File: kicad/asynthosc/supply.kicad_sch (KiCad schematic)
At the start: 50 parts, among them J1 USB_B_Micro, J2 Conn_02x05_Odd_Even, U1 LM1117S-3.3, U2 LMR62421XMF, U3 USBLC6-2SC6, U4 LM1117S-5.0, U5 Si1869DH

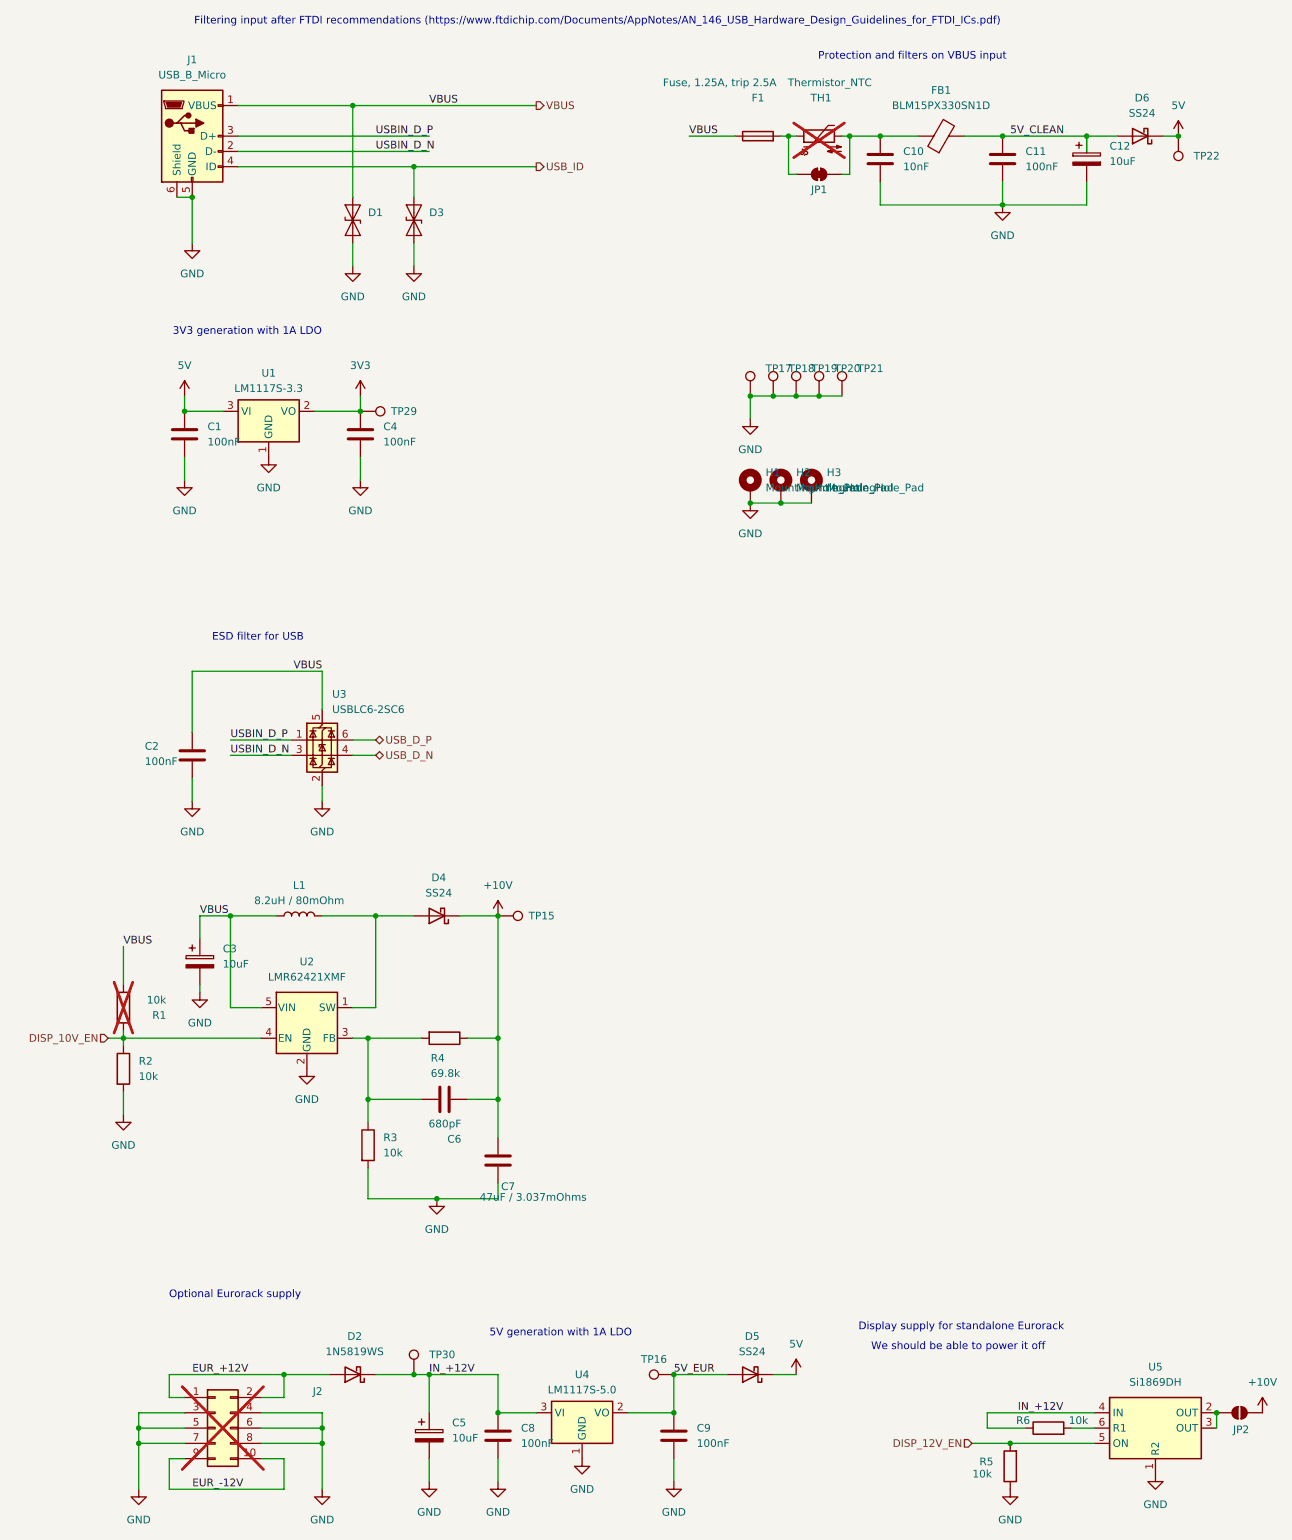
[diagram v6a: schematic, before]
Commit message: pcb: route, add some silkscreen
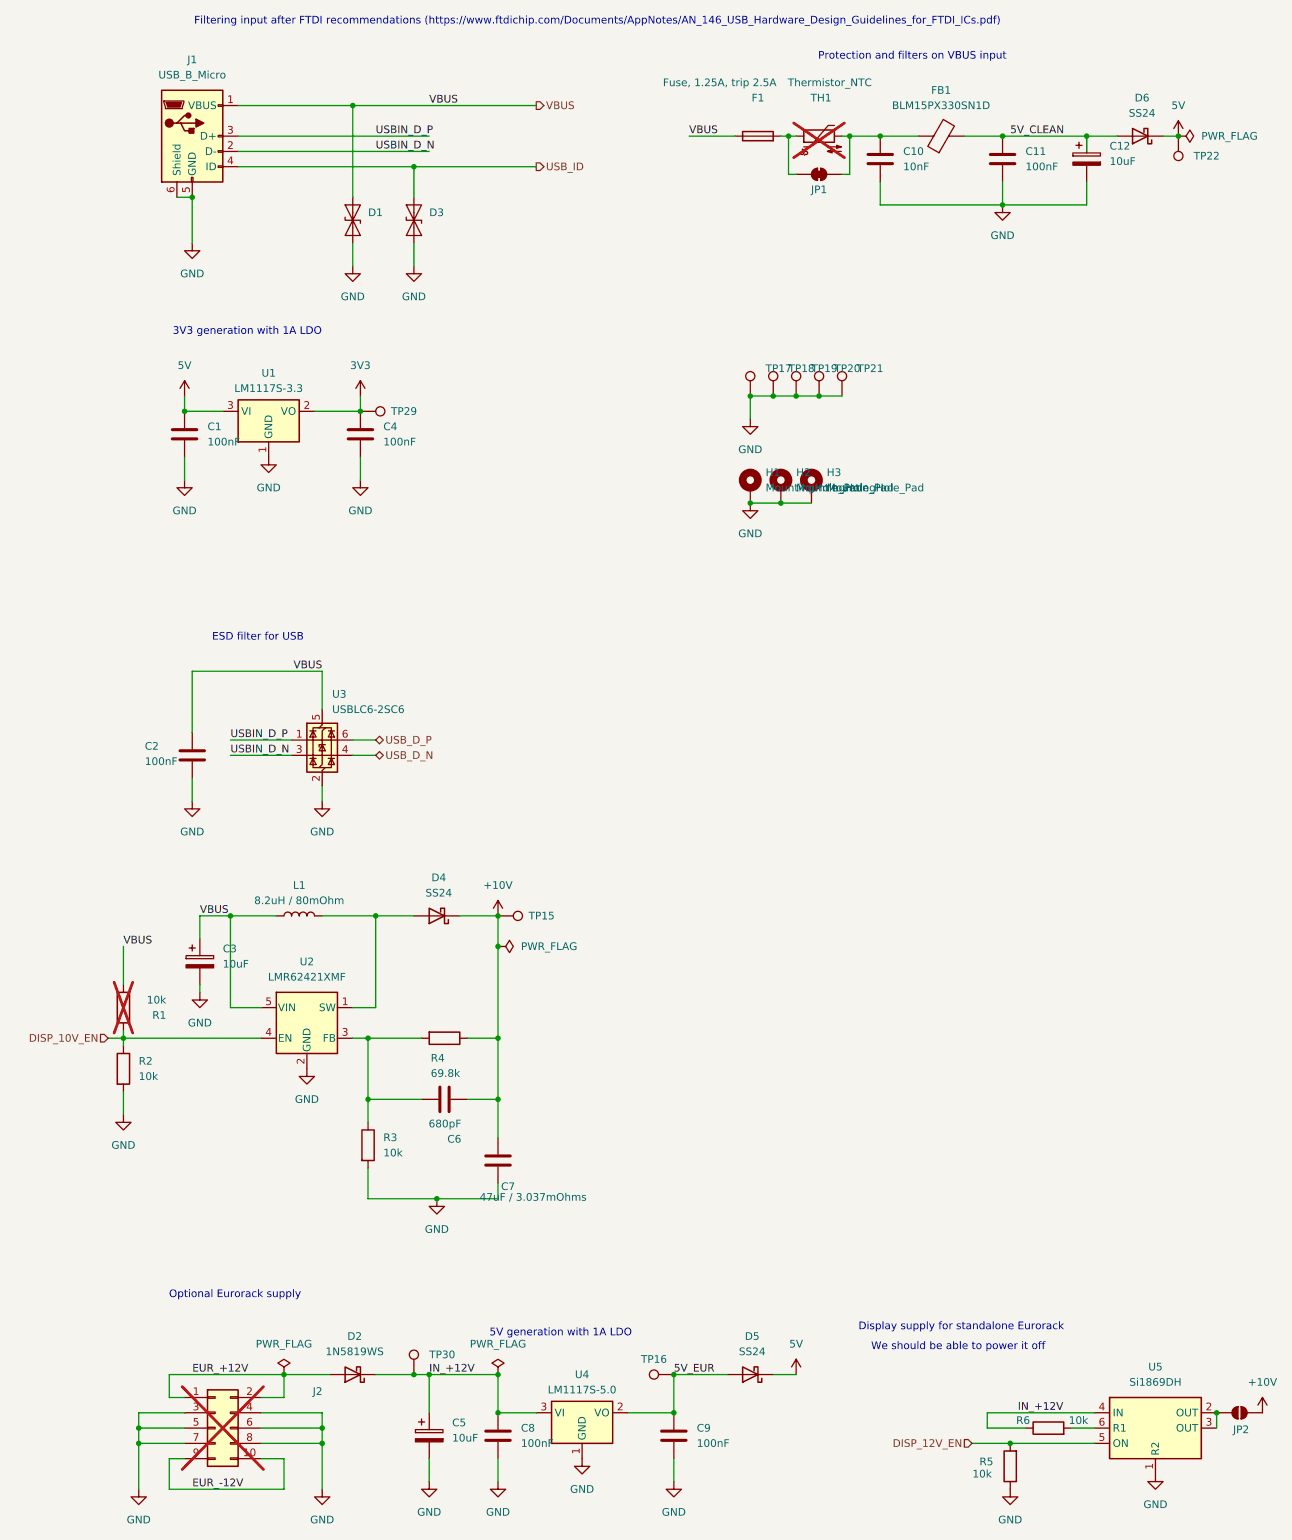
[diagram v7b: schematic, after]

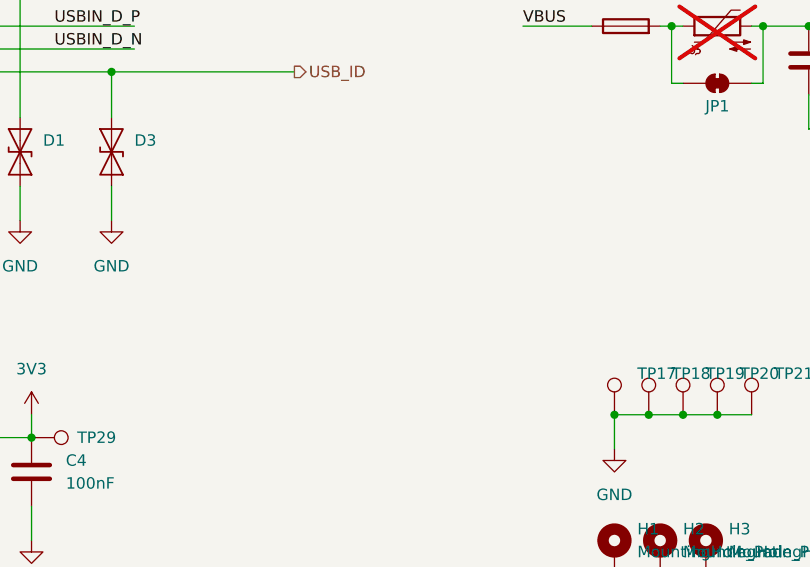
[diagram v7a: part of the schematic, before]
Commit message: comp: add vertical usb micro-b and rj45 footprints
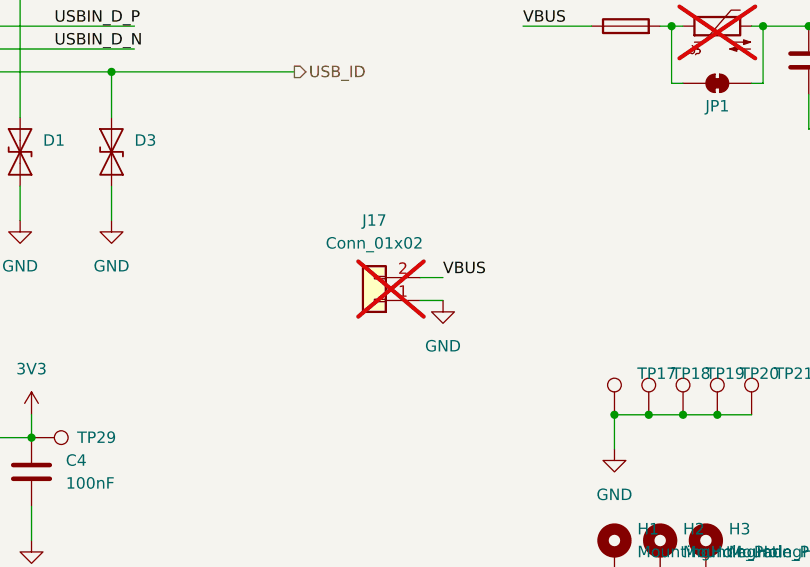
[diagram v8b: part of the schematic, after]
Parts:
- added J17: Conn_01x02, Connector_PinHeader_2.54mm:PinHeader_1x02_P2.54mm_Vertical, symbol Connector_Generic:Conn_01x02
- J1: footprint asynthosc:USB_Micro-B_Shou-han-MicroXNJ -> asynthosc:USB_Micro-B_Hanxia_HX_MICRO_180D_ZB; Manufacturer ShouHan -> Hanxia; RefNum MicroXNJ -> HX MICRO 180D ZB
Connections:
- net GND: now also J17.1 (Pin_1)
- net VBUS: now also J17.2 (Pin_2)
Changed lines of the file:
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@@
 	(wire
 		(pts
+			(xy 111.76 71.12) (xy 114.3 71.12)
+		)
+		(stroke
+			(width 0)
+			(type default)
+		)
+	)
+	(wire
+		(pts
 			(xy 67.31 60.96) (xy 67.31 64.77)
 		)
@@
 	(wire
 		(pts
+			(xy 111.76 73.66) (xy 114.3 73.66)
+		)
+		(stroke
+			(width 0)
+			(type default)
+		)
+	)
+	(wire
+		(pts
 			(xy 154.94 50.8) (xy 154.94 54.61)
 		)
@@
 	)
 	(label "VBUS"
+		(at 114.3 71.12 0)
+		(fields_autoplaced yes)
+		(effects
+			(font
+				(size 1.27 1.27)
+			)
+			(justify left bottom)
+		)
+	)
+	(label "VBUS"
 		(at 80.01 38.1 0)
 		(fields_autoplaced yes)
@@
 	)
 	(symbol
+		(lib_id "Connector_Generic:Conn_01x02")
+		(at 106.68 73.66 180)
+		(unit 1)
+		(exclude_from_sim yes)
+		(in_bom no)
+		(on_board yes)
+		(dnp yes)
+		(fields_autoplaced yes)
+		(property "Reference" "J17"
+			(at 106.68 64.77 0)
+			(effects
+				(font
+					(size 1.27 1.27)
+				)
+			)
+		)
+		(property "Value" "Conn_01x02"
+			(at 106.68 67.31 0)
+			(effects
+				(font
+					(size 1.27 1.27)
+				)
+			)
+		)
+		(property "Footprint" "Connector_PinHeader_2.54mm:PinHeader_1x02_P2.54mm_Vertical"
+			(at 106.68 73.66 0)
+			(effects
+				(font
+					(size 1.27 1.27)
+				)
+				(hide yes)
+			)
+		)
+		(property "Datasheet" "~"
+			(at 106.68 73.66 0)
+			(effects
+				(font
+					(size 1.27 1.27)
+				)
+				(hide yes)
+			)
+		)
+		(property "Description" "Generic connector, single row, 01x02, script generated (kicad-library-utils/schlib/autogen/connector/)"
+			(at 106.68 73.66 0)
+			(effects
+				(font
+					(size 1.27 1.27)
+				)
+				(hide yes)
+			)
+		)
+		(pin "2"
+		)
+		(pin "1"
+		)
+		(instances
+			(project ""
+				(path "/d73e377a-a016-415f-8824-91cc6e4907b9/22ca5166-338c-4a24-8f8a-545e4a0286bf"
+					(reference "J17")
+					(unit 1)
+				)
+			)
+		)
+	)
+	(symbol
 		(lib_id "power:PWR_FLAG")
 		(at 55.88 248.92 0)
@@
 	)
 	(symbol
+		(lib_id "power:GND")
+		(at 114.3 73.66 0)
+		(unit 1)
+		(exclude_from_sim no)
+		(in_bom yes)
+		(on_board yes)
+		(dnp no)
+		(fields_autoplaced yes)
+		(property "Reference" "#PWR0160"
+			(at 114.3 80.01 0)
+			(effects
+				(font
+					(size 1.27 1.27)
+				)
+				(hide yes)
+			)
+		)
+		(property "Value" "GND"
+			(at 114.3 78.74 0)
+			(effects
+				(font
+					(size 1.27 1.27)
+				)
+			)
+		)
+		(property "Footprint" ""
+			(at 114.3 73.66 0)
+			(effects
+				(font
+					(size 1.27 1.27)
+				)
+				(hide yes)
+			)
+		)
+		(property "Datasheet" ""
+			(at 114.3 73.66 0)
+			(effects
+				(font
+					(size 1.27 1.27)
+				)
+				(hide yes)
+			)
+		)
+		(property "Description" "Power symbol creates a global label with name \"GND\" , ground"
+			(at 114.3 73.66 0)
+			(effects
+				(font
+					(size 1.27 1.27)
+				)
+				(hide yes)
+			)
+		)
+		(pin "1"
+		)
+		(instances
+			(project "asynthosc"
+				(path "/d73e377a-a016-415f-8824-91cc6e4907b9/22ca5166-338c-4a24-8f8a-545e4a0286bf"
+					(reference "#PWR0160")
+					(unit 1)
+				)
+			)
+		)
+	)
+	(symbol
 		(lib_id "Power_Protection:USBLC6-2SC6")
 		(at 62.23 143.51 0)
@@
 			)
 		)
-		(property "Footprint" "asynthosc:USB_Micro-B_Shou-han-MicroXNJ"
+		(property "Footprint" "asynthosc:USB_Micro-B_Hanxia_HX_MICRO_180D_ZB"
 			(at 44.45 44.45 0)
 			(effects
@@
 			)
 		)
-		(property "Manufacturer" "ShouHan"
+		(property "Manufacturer" "Hanxia"
 			(at 40.64 43.18 0)
 			(effects
@@
 			)
 		)
-		(property "RefNum" "MicroXNJ"
+		(property "RefNum" " HX MICRO 180D ZB"
 			(at 40.64 43.18 0)
 			(effects
